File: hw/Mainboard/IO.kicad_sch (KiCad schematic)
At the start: 6 parts, among them U7 W65C21N, U8 W65C21N, U9 W65C22N

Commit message: hw: wip
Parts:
- added PT6, PT7, PT8: PowerTie_2, PET:NetTie-2_SMD_Pad_1.6_to_0.4mm, symbol PET:PowerTie_2
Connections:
- net +5V: now also PT6.1, PT7.1, PT8.1; no longer U7.24 (CS1), U8.24 (CS1), U9.24 (CS1)
- net GND: no longer U7.1 (VSS), U8.1 (VSS), U9.1 (VSS)
- new net: PT8.2, U8.24 (CS1)
- new net: PT7.2, U9.24 (CS1)
- new net: PT6.2, U7.24 (CS1)
- new net PD_GND: U7.1 (VSS), U8.1 (VSS), U9.1 (VSS)
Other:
- moved on the sheet: C7, C8, C9

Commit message: hw: wip
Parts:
- C7, C8, C9: LCSC C1525 -> C307331
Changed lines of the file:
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@@
       (effects (font (size 1.27 1.27)) hide)
     )
-    (property "Datasheet" "https://datasheet.lcsc.com/lcsc/1810191219_Samsung-Electro-Mechanics-CL05B104KO5NNNC_C1525.pdf" (id 3) (at 93.98 118.11 0)
+    (property "Datasheet" "" (id 3) (at 93.98 118.11 0)
       (effects (font (size 1.27 1.27)) hide)
     )
-    (property "LCSC" "C1525" (id 4) (at 93.98 118.11 0)
+    (property "LCSC" "C307331" (id 4) (at 93.98 118.11 0)
       (effects (font (size 1.27 1.27)) hide)
     )
@@
       (effects (font (size 1.27 1.27)) hide)
     )
-    (property "Datasheet" "https://datasheet.lcsc.com/lcsc/1810191219_Samsung-Electro-Mechanics-CL05B104KO5NNNC_C1525.pdf" (id 3) (at 93.98 22.86 0)
+    (property "Datasheet" "" (id 3) (at 93.98 22.86 0)
       (effects (font (size 1.27 1.27)) hide)
     )
-    (property "LCSC" "C1525" (id 4) (at 93.98 22.86 0)
+    (property "LCSC" "C307331" (id 4) (at 93.98 22.86 0)
       (effects (font (size 1.27 1.27)) hide)
     )
@@
       (effects (font (size 1.27 1.27)) hide)
     )
-    (property "Datasheet" "https://datasheet.lcsc.com/lcsc/1810191219_Samsung-Electro-Mechanics-CL05B104KO5NNNC_C1525.pdf" (id 3) (at 191.77 91.44 0)
+    (property "Datasheet" "" (id 3) (at 191.77 91.44 0)
       (effects (font (size 1.27 1.27)) hide)
     )
-    (property "LCSC" "C1525" (id 4) (at 191.77 91.44 0)
+    (property "LCSC" "C307331" (id 4) (at 191.77 91.44 0)
       (effects (font (size 1.27 1.27)) hide)
     )

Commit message: wip
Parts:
- added PT55: PowerTie_2, PET:NetTie-2_SMD_Pad_1.6_to_0.4mm, symbol PET:PowerTie_2
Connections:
- net +5V: now also PT55.1; no longer C9.1
- net Bϕ2 renamed BPHI2
- new net: C9.1, PT55.2
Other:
- moved on the sheet: C9
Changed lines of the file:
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@@
+    (stroke (width 0) (type default) (color 0 0 0 0))
+  )
+  (wire (pts (xy 87.63 22.86) (xy 86.36 22.86))
     (stroke (width 0) (type default) (color 0 0 0 0))
   )
@@
     (stroke (width 0) (type default) (color 0 0 0 0))
   )
-  (wire (pts (xy 101.6 22.86) (xy 96.52 22.86))
+  (wire (pts (xy 101.6 22.86) (xy 97.79 22.86))
     (stroke (width 0) (type default) (color 0 0 0 0))
   )
@@
   )
   (bus (pts (xy 30.48 71.12) (xy 53.34 71.12))
-    (stroke (width 0) (type default) (color 0 0 0 0))
-  )
-  (wire (pts (xy 86.36 22.86) (xy 91.44 22.86))
     (stroke (width 0) (type default) (color 0 0 0 0))
   )
@@
     (effects (font (size 1.27 1.27)) (justify left))
   )
-  (hierarchical_label "Bϕ2" (shape input) (at 30.48 102.87 180)
+  (hierarchical_label "BPHI2" (shape input) (at 30.48 102.87 180)
     (effects (font (size 1.27 1.27)) (justify right))
   )
@@
       (effects (font (size 1.27 1.27)) hide)
     )
-    (property "Datasheet" "" (id 3) (at 86.36 149.86 0)
+    (property "Datasheet" "https://www.mouser.com/datasheet/2/436/w65c21-661.pdf" (id 3) (at 86.36 149.86 0)
       (effects (font (size 1.27 1.27)) hide)
     )
@@
       (effects (font (size 1.27 1.27)) hide)
     )
-    (property "Datasheet" "" (id 3) (at 184.15 124.46 0)
+    (property "Datasheet" "https://www.mouser.com/datasheet/2/436/w65c22-1197.pdf" (id 3) (at 184.15 124.46 0)
       (effects (font (size 1.27 1.27)) hide)
     )
@@
       (effects (font (size 1.27 1.27)) hide)
     )
-    (property "Datasheet" "" (id 3) (at 86.36 54.61 0)
+    (property "Datasheet" "https://www.mouser.com/datasheet/2/436/w65c21-661.pdf" (id 3) (at 86.36 54.61 0)
       (effects (font (size 1.27 1.27)) hide)
     )
@@
     (pin "2")
   )
-  (symbol (lib_id "Device:C_Small") (at 93.98 22.86 90) (unit 1)
+  (symbol (lib_id "Device:C_Small") (at 95.25 22.86 90) (unit 1)
     (in_bom yes) (on_board yes)
-    (property "Reference" "C9" (id 0) (at 93.98 16.51 90)
+    (property "Reference" "C9" (id 0) (at 95.25 16.51 90)
       (effects (font (size 1.27 1.27)) (justify left))
     )
-    (property "Value" "100n" (id 1) (at 96.52 19.05 90)
+    (property "Value" "100n" (id 1) (at 97.79 19.05 90)
       (effects (font (size 1.27 1.27)) (justify left))
     )
-    (property "Footprint" "Capacitor_SMD:C_0402_1005Metric" (id 2) (at 93.98 22.86 0)
-      (effects (font (size 1.27 1.27)) hide)
-    )
-    (property "Datasheet" "https://datasheet.lcsc.com/lcsc/2304140030_Samsung-Electro-Mechanics-CL05B104KB54PNC_C307331.pdf" (id 3) (at 93.98 22.86 0)
-      (effects (font (size 1.27 1.27)) hide)
-    )
-    (property "LCSC" "C307331" (id 4) (at 93.98 22.86 0)
+    (property "Footprint" "Capacitor_SMD:C_0402_1005Metric" (id 2) (at 95.25 22.86 0)
+      (effects (font (size 1.27 1.27)) hide)
+    )
+    (property "Datasheet" "https://datasheet.lcsc.com/lcsc/2304140030_Samsung-Electro-Mechanics-CL05B104KB54PNC_C307331.pdf" (id 3) (at 95.25 22.86 0)
+      (effects (font (size 1.27 1.27)) hide)
+    )
+    (property "LCSC" "C307331" (id 4) (at 95.25 22.86 0)
       (effects (font (size 1.27 1.27)) hide)
     )
@@
     (pin "1")
   )
+  (symbol (lib_id "PET:PowerTie_2") (at 90.17 22.86 0) (unit 1)
+    (in_bom yes) (on_board yes) (fields_autoplaced)
+    (property "Reference" "PT55" (id 0) (at 90.17 20.955 0)
+      (effects (font (size 1.27 1.27)) hide)
+    )
+    (property "Value" "PowerTie_2" (id 1) (at 90.17 24.765 0)
+      (effects (font (size 1.27 1.27)) hide)
+    )
+    (property "Footprint" "PET:NetTie-2_SMD_Pad_1.6_to_0.4mm" (id 2) (at 90.17 22.86 0)
+      (effects (font (size 1.27 1.27)) hide)
+    )
+    (property "Datasheet" "~" (id 3) (at 90.17 22.86 0)
+      (effects (font (size 1.27 1.27)) hide)
+    )
+    (pin "1")
+    (pin "2")
+  )
   (symbol (lib_id "PET:PowerTie_2") (at 68.58 143.51 0) (unit 1)
     (in_bom yes) (on_board yes) (fields_autoplaced)
@@
       (effects (font (size 1.27 1.27)) hide)
     )
-    (property "Datasheet" "" (id 3) (at 68.58 143.51 0)
+    (property "Datasheet" "~" (id 3) (at 68.58 143.51 0)
       (effects (font (size 1.27 1.27)) hide)
     )
@@
       (effects (font (size 1.27 1.27)) hide)
     )
-    (property "Datasheet" "" (id 3) (at 166.37 113.03 0)
+    (property "Datasheet" "~" (id 3) (at 166.37 113.03 0)
       (effects (font (size 1.27 1.27)) hide)
     )
@@
       (effects (font (size 1.27 1.27)) hide)
     )
-    (property "Datasheet" "" (id 3) (at 68.58 48.26 0)
-      (effects (font (size 1.27 1.27)) hide)
-    )
+    (property "Datasheet" "~" (id 3) (at 68.58 48.26 0)
+      (effects (font (size 1.27 1.27)) hide)
+    )

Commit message: hw: routing / silk wip
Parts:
- added PT56: PowerTie_2, PET:NetTie-2_SMD_Pad_1.6_to_0.4mm, symbol PET:PowerTie_2
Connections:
- net +5V: now also PT56.1; no longer C8.1
- new net: C8.1, PT56.2
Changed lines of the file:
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@@
-    (stroke (width 0) (type default) (color 0 0 0 0))
-  )
-  (wire (pts (xy 184.15 91.44) (xy 189.23 91.44))
     (stroke (width 0) (type default) (color 0 0 0 0))
   )
@@
       (effects (font (size 1.27 1.27)) hide)
     )
+    (pin "1")
+    (pin "2")
+  )
+  (symbol (lib_id "PET:PowerTie_2") (at 186.69 91.44 0) (unit 1)
+    (in_bom yes) (on_board yes) (fields_autoplaced)
+    (property "Reference" "PT56" (id 0) (at 186.69 89.535 0)
+      (effects (font (size 1.27 1.27)) hide)
+    )
+    (property "Value" "PowerTie_2" (id 1) (at 186.69 93.345 0)
+      (effects (font (size 1.27 1.27)) hide)
+    )
+    (property "Footprint" "PET:NetTie-2_SMD_Pad_1.6_to_0.4mm" (id 2) (at 186.69 91.44 0)
+      (effects (font (size 1.27 1.27)) hide)
+    )
+    (property "Datasheet" "~" (id 3) (at 186.69 91.44 0)
+      (effects (font (size 1.27 1.27)) hide)
+    )

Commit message: hw: PN for IC, remove dup PNs, remove redundant headroom text on PWR
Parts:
- U7, U8: DIGI-KEY AE10008-ND -> (none); MOUSER 955-W65C21N6TPG-14 -> 955-W65C21N6TPG-14,571-1-2199299-5
- U9: DIGI-KEY AE10008-ND -> (none); MOUSER 955-W65C22N6TPG-14 -> 955-W65C22N6TPG-14,571-1-2199299-5
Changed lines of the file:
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@@
       (effects (font (size 1.27 1.27)) hide)
     )
-    (property "MOUSER" "955-W65C21N6TPG-14" (id 4) (at 86.36 153.67 0)
-      (effects (font (size 1.27 1.27)) hide)
-    )
-    (property "DIGI-KEY" "AE10008-ND" (id 5) (at 86.36 153.67 0)
+    (property "MOUSER" "955-W65C21N6TPG-14,571-1-2199299-5" (id 4) (at 86.36 153.67 0)
       (effects (font (size 1.27 1.27)) hide)
     )
@@
       (effects (font (size 1.27 1.27)) hide)
     )
-    (property "MOUSER" "955-W65C22N6TPG-14" (id 4) (at 184.15 128.27 0)
-      (effects (font (size 1.27 1.27)) hide)
-    )
-    (property "DIGI-KEY" "AE10008-ND" (id 5) (at 184.15 128.27 0)
+    (property "MOUSER" "955-W65C22N6TPG-14,571-1-2199299-5" (id 4) (at 184.15 128.27 0)
       (effects (font (size 1.27 1.27)) hide)
     )
@@
       (effects (font (size 1.27 1.27)) hide)
     )
-    (property "MOUSER" "955-W65C21N6TPG-14" (id 4) (at 86.36 58.42 0)
+    (property "MOUSER" "955-W65C21N6TPG-14,571-1-2199299-5" (id 4) (at 86.36 58.42 0)
       (effects (font (size 1.27 1.27)) hide)
     )
-    (property "DIGI-KEY" "AE10008-ND" (id 5) (at 86.36 58.42 0)
-      (effects (font (size 1.27 1.27)) hide)
-    )

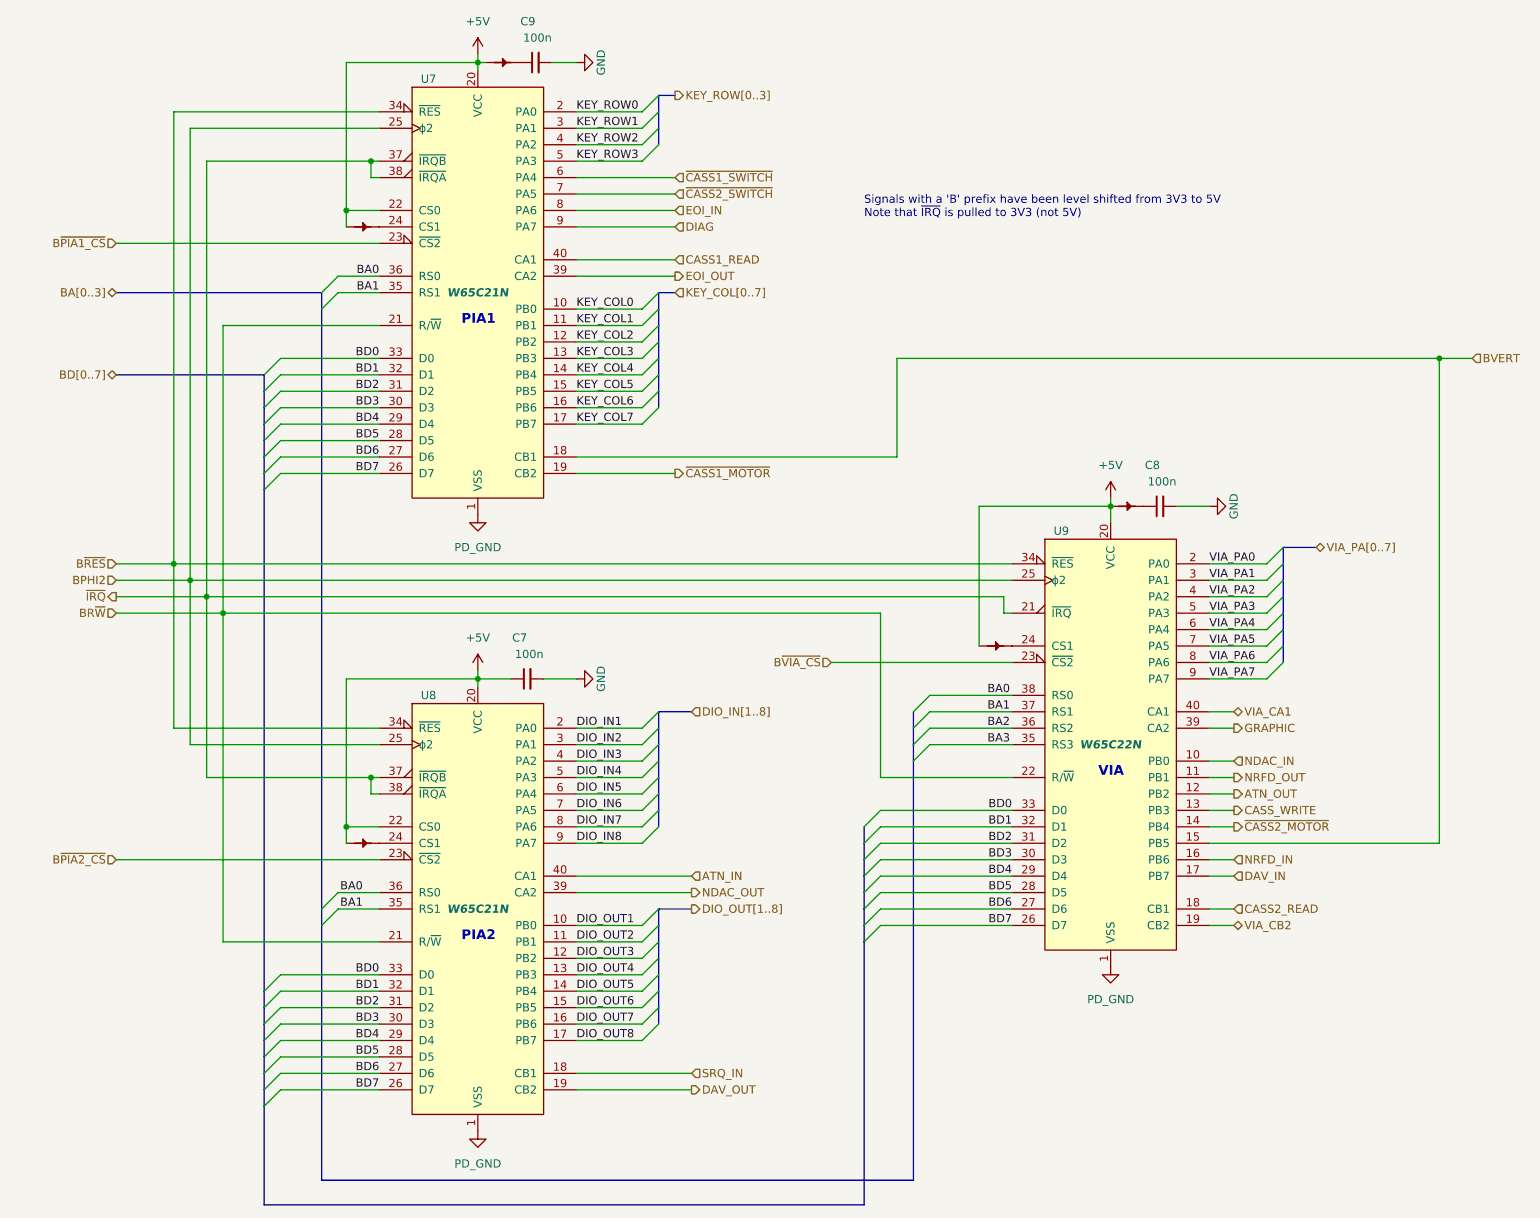
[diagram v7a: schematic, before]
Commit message: hw: 9V DC plug on left edge, change default track size
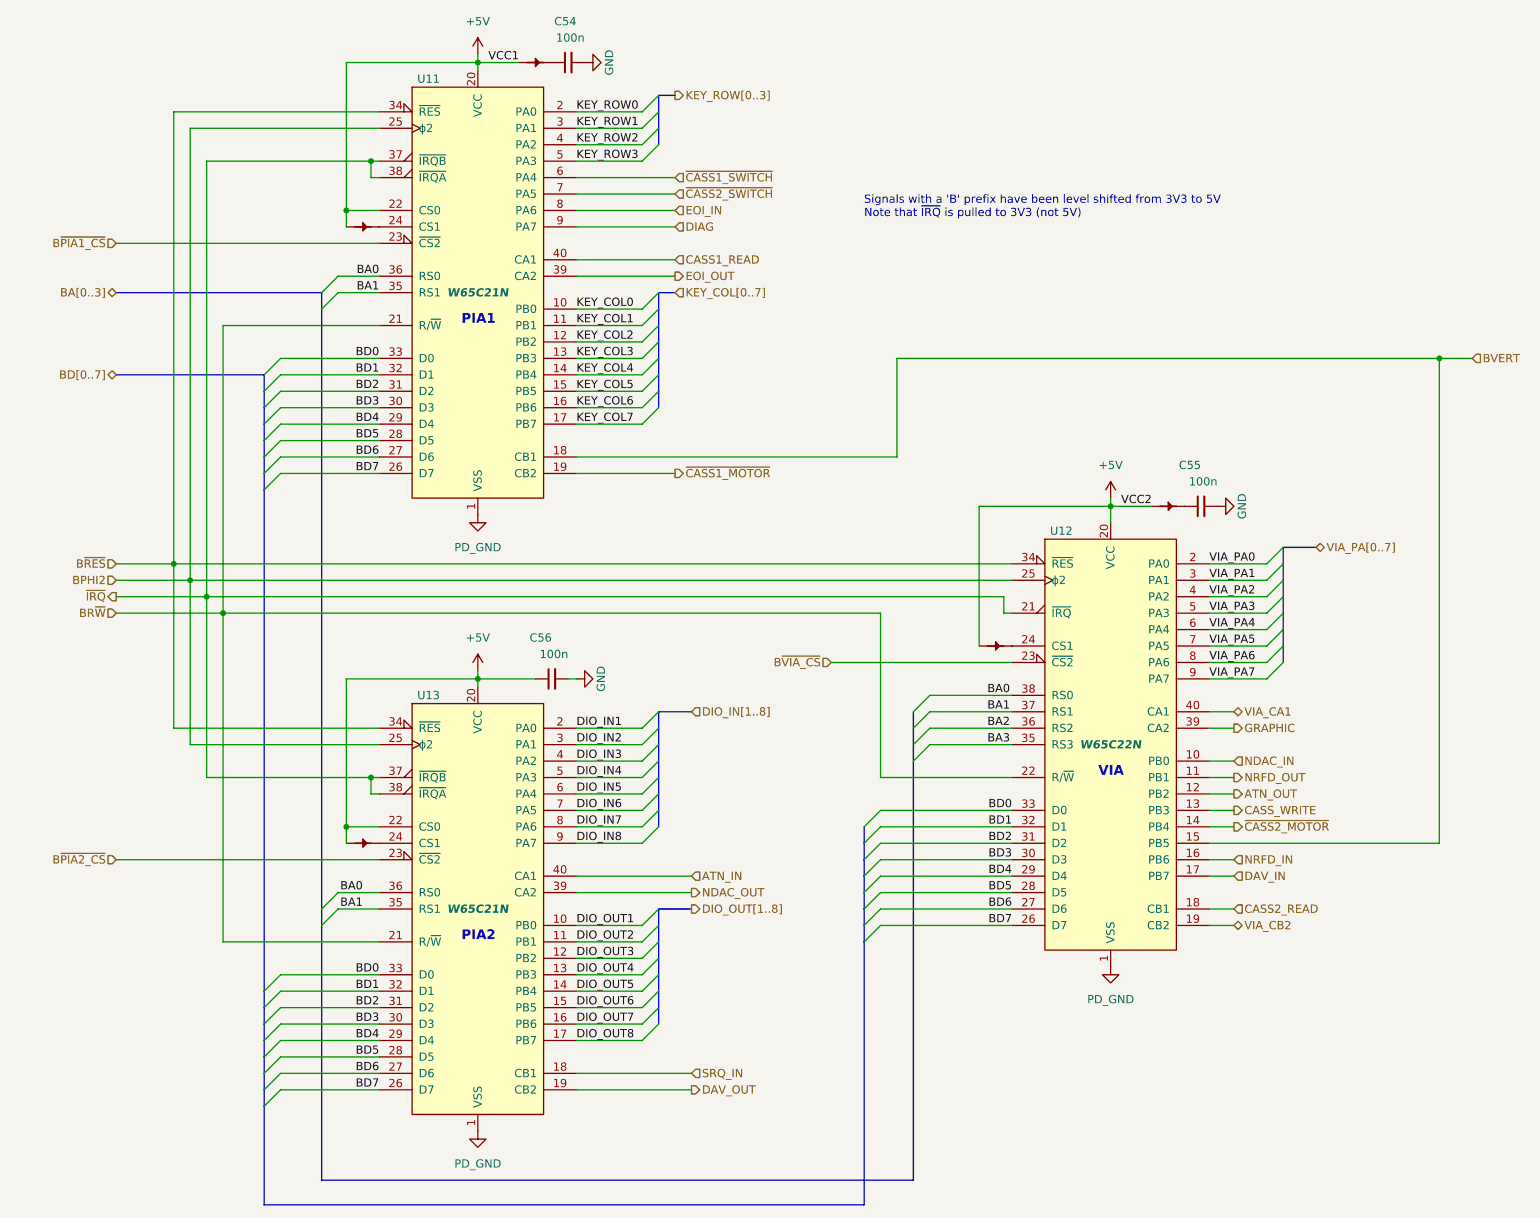
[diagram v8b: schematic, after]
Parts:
- renumbered C9 to C54, C8 to C55, C7 to C56, PT55 to PT31, PT6 to PT32, PT56 to PT33, PT7 to PT34, PT8 to PT35, U7 to U11, U9 to U12, U8 to U13
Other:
- moved on the sheet: C54, C55, C56
